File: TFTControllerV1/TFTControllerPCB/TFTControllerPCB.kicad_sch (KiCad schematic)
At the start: 17 parts, among them J1 Conn_01x40, J2 Conn_02x04_Counter_Clockwise, J3 Conn_02x04_Counter_Clockwise, J4 Conn_02x03_Counter_Clockwise, J5 Conn_02x03_Counter_Clockwise, Q1 BSS138, Q2 BSS138, SW1 SW_Push, U1 STM32F107VCTx, U2 XPT2046TS

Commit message: working touch
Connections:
- net XPT_CS: now reaches U2.15 (~{CS})
- net XPT_CS: now also U1.62 (PD15)
- net SWDIO: now reaches U1.72 (PA13)
- net SWCLK: now reaches U1.76 (PA14)
- net SCK: now reaches U1.78 (PC10)
- net MISO: now reaches U1.79 (PC11)
- net MOSI: now reaches U1.80 (PC12)
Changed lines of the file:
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@@
+		)
+	)
+	(global_label "XPT_CS"
+		(shape input)
+		(at 163.83 170.18 180)
+		(fields_autoplaced yes)
+		(effects
+			(font
+				(size 1.27 1.27)
+			)
+			(justify right)
+		)
+		(property "Intersheetrefs" "${INTERSHEET_REFS}"
+			(at 153.9506 170.18 0)
+			(effects
+				(font
+					(size 1.27 1.27)
+				)
+				(justify right)
+				(hide yes)
+			)
+		)
+	)
+	(global_label "MOSI"
+		(shape input)
+		(at 214.63 180.34 0)
+		(fields_autoplaced yes)
+		(effects
+			(font
+				(size 1.27 1.27)
+			)
+			(justify left)
+		)
+		(property "Intersheetrefs" "${INTERSHEET_REFS}"
+			(at 222.2114 180.34 0)
+			(effects
+				(font
+					(size 1.27 1.27)
+				)
+				(justify left)
+				(hide yes)
+			)
+		)
+	)
+	(global_label "MISO"
+		(shape input)
+		(at 214.63 177.8 0)
+		(fields_autoplaced yes)
+		(effects
+			(font
+				(size 1.27 1.27)
+			)
+			(justify left)
+		)
+		(property "Intersheetrefs" "${INTERSHEET_REFS}"
+			(at 222.2114 177.8 0)
+			(effects
+				(font
+					(size 1.27 1.27)
+				)
+				(justify left)
+				(hide yes)
+			)
+		)
+	)
+	(global_label "SWDIO"
+		(shape input)
+		(at 214.63 96.52 0)
+		(fields_autoplaced yes)
+		(effects
+			(font
+				(size 1.27 1.27)
+			)
+			(justify left)
+		)
+		(property "Intersheetrefs" "${INTERSHEET_REFS}"
+			(at 223.4814 96.52 0)
+			(effects
+				(font
+					(size 1.27 1.27)
+				)
+				(justify left)
+				(hide yes)
+			)
+		)
+	)
+	(global_label "SCK"
+		(shape input)
+		(at 214.63 175.26 0)
+		(fields_autoplaced yes)
+		(effects
+			(font
+				(size 1.27 1.27)
+			)
+			(justify left)
+		)
+		(property "Intersheetrefs" "${INTERSHEET_REFS}"
+			(at 221.3647 175.26 0)
+			(effects
+				(font
+					(size 1.27 1.27)
+				)
+				(justify left)
+				(hide yes)
+			)
+		)
+	)
+	(global_label "SWCLK"
+		(shape input)
+		(at 214.63 99.06 0)
+		(fields_autoplaced yes)
+		(effects
+			(font
+				(size 1.27 1.27)
+			)
+			(justify left)
+		)
+		(property "Intersheetrefs" "${INTERSHEET_REFS}"
+			(at 223.8442 99.06 0)
+			(effects
+				(font
+					(size 1.27 1.27)
+				)
+				(justify left)
+				(hide yes)
+			)
+		)
+	)
+	(global_label "XPT_CS"
+		(shape input)
+		(at 241.3 92.71 180)
+		(fields_autoplaced yes)
+		(effects
+			(font
+				(size 1.27 1.27)
+			)
+			(justify right)
+		)
+		(property "Intersheetrefs" "${INTERSHEET_REFS}"
+			(at 231.4206 92.71 0)
+			(effects
+				(font
+					(size 1.27 1.27)
+				)
+				(justify right)
+				(hide yes)
+			)
 		)
 	)

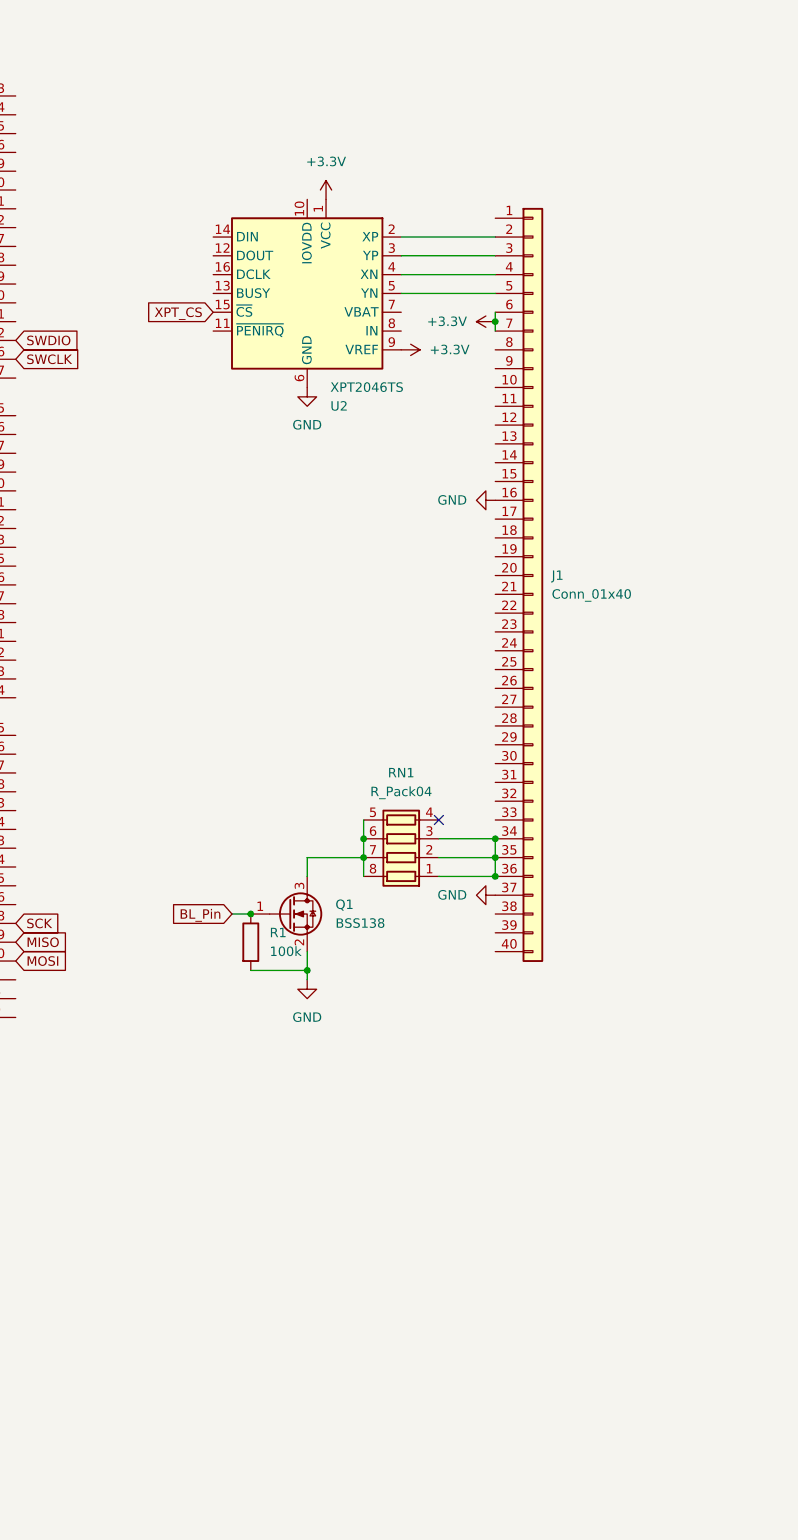
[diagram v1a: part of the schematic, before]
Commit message: migrate project to newer MX version
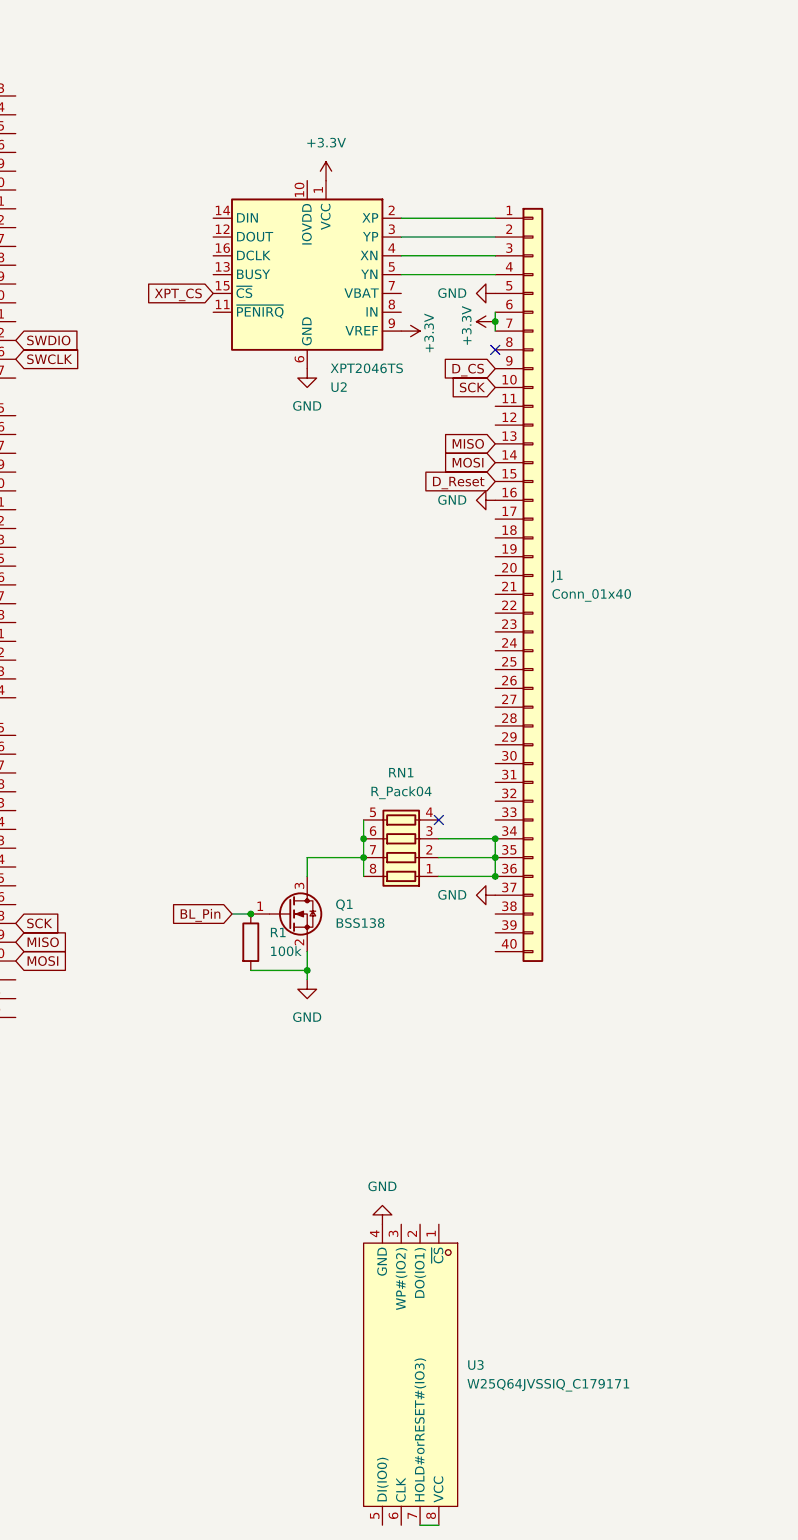
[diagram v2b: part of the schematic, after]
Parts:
- added U3: W25Q64JVSSIQ_C179171, easyeda2kicad:SOIC-8_L5.3-W5.3-P1.27-LS8.0-BL, symbol easyeda2kicad:W25Q64JVSSIQ_C179171
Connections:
- net GND: now also J1.5 (Pin_5), U3.4 (GND)
- net MISO: now also J1.13 (Pin_13)
- net MOSI: now also J1.14 (Pin_14)
- net SCK: now also J1.10 (Pin_10)
- net at U2.2 (XP): now also J1.1 (Pin_1); no longer J1.2 (Pin_2)
- net at U2.3 (YP): now also J1.2 (Pin_2); no longer J1.3 (Pin_3)
- net at U2.4 (XN): now also J1.3 (Pin_3); no longer J1.4 (Pin_4)
- net at U2.5 (YN): now also J1.4 (Pin_4); no longer J1.5 (Pin_5)
- net D_Reset: now reaches J1.15 (Pin_15)
- net D_CS: now reaches J1.9 (Pin_9)
- new net: U3.7 (HOLD#orRESET#(IO3)), U3.8 (VCC)
- no-connect marks 3 -> 4
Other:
- moved on the sheet: U2

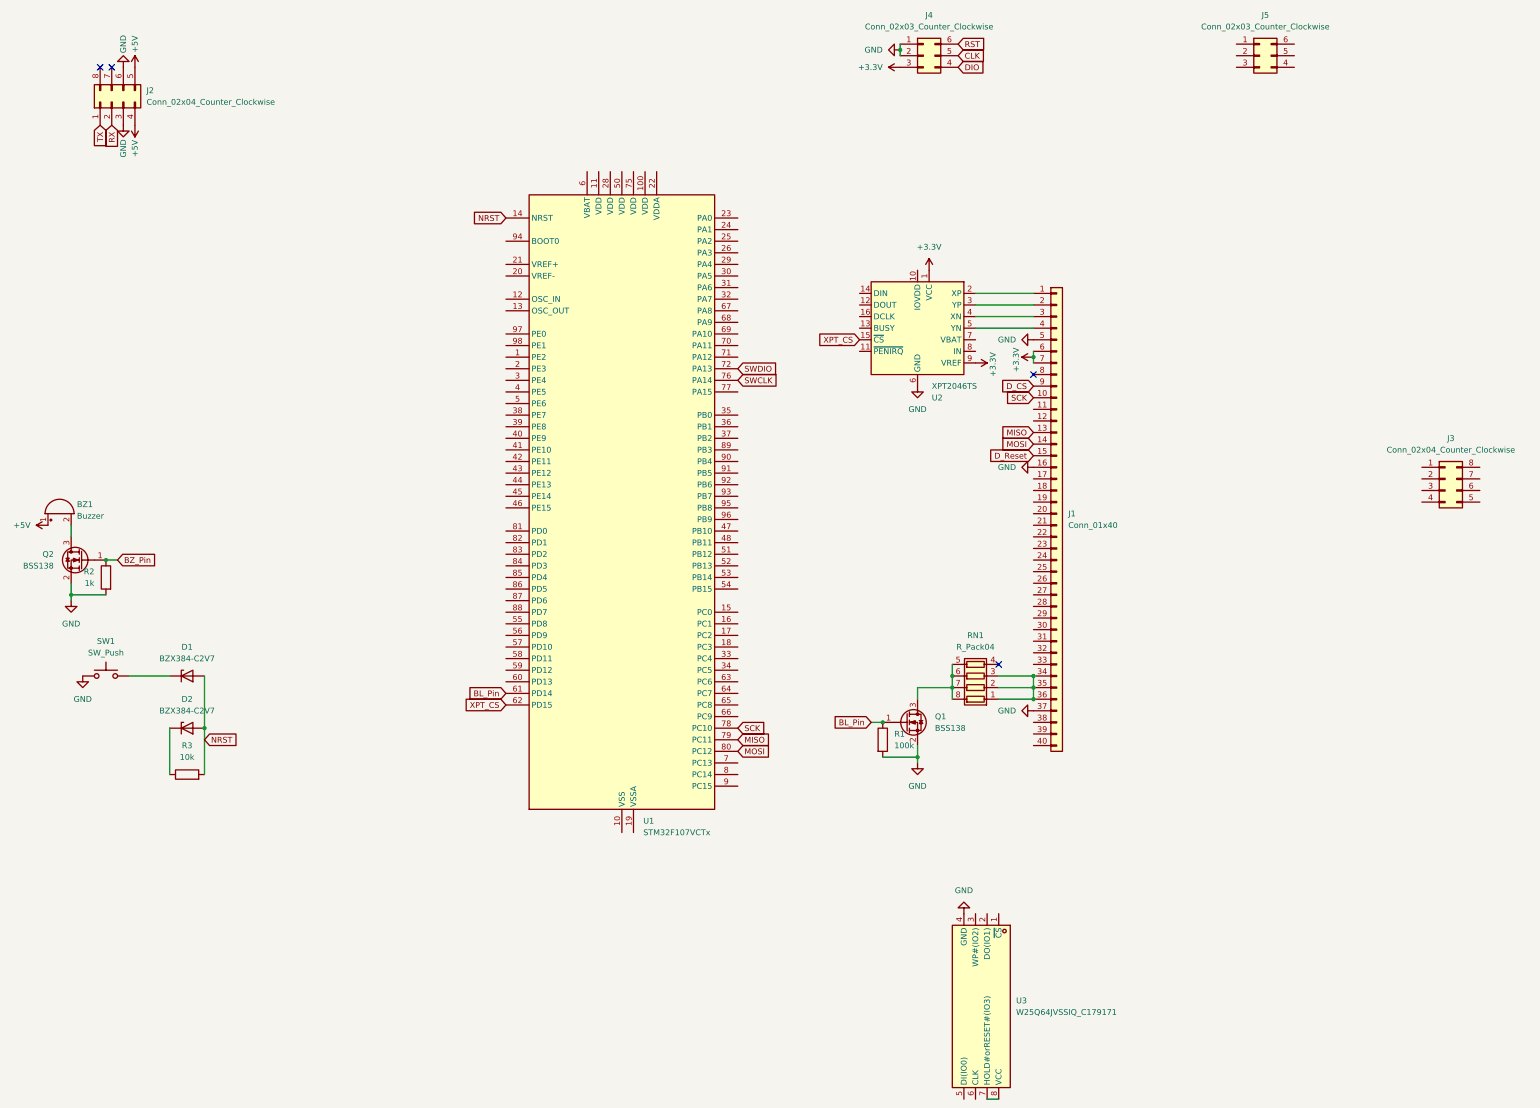
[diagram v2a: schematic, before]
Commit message: add 2SPI
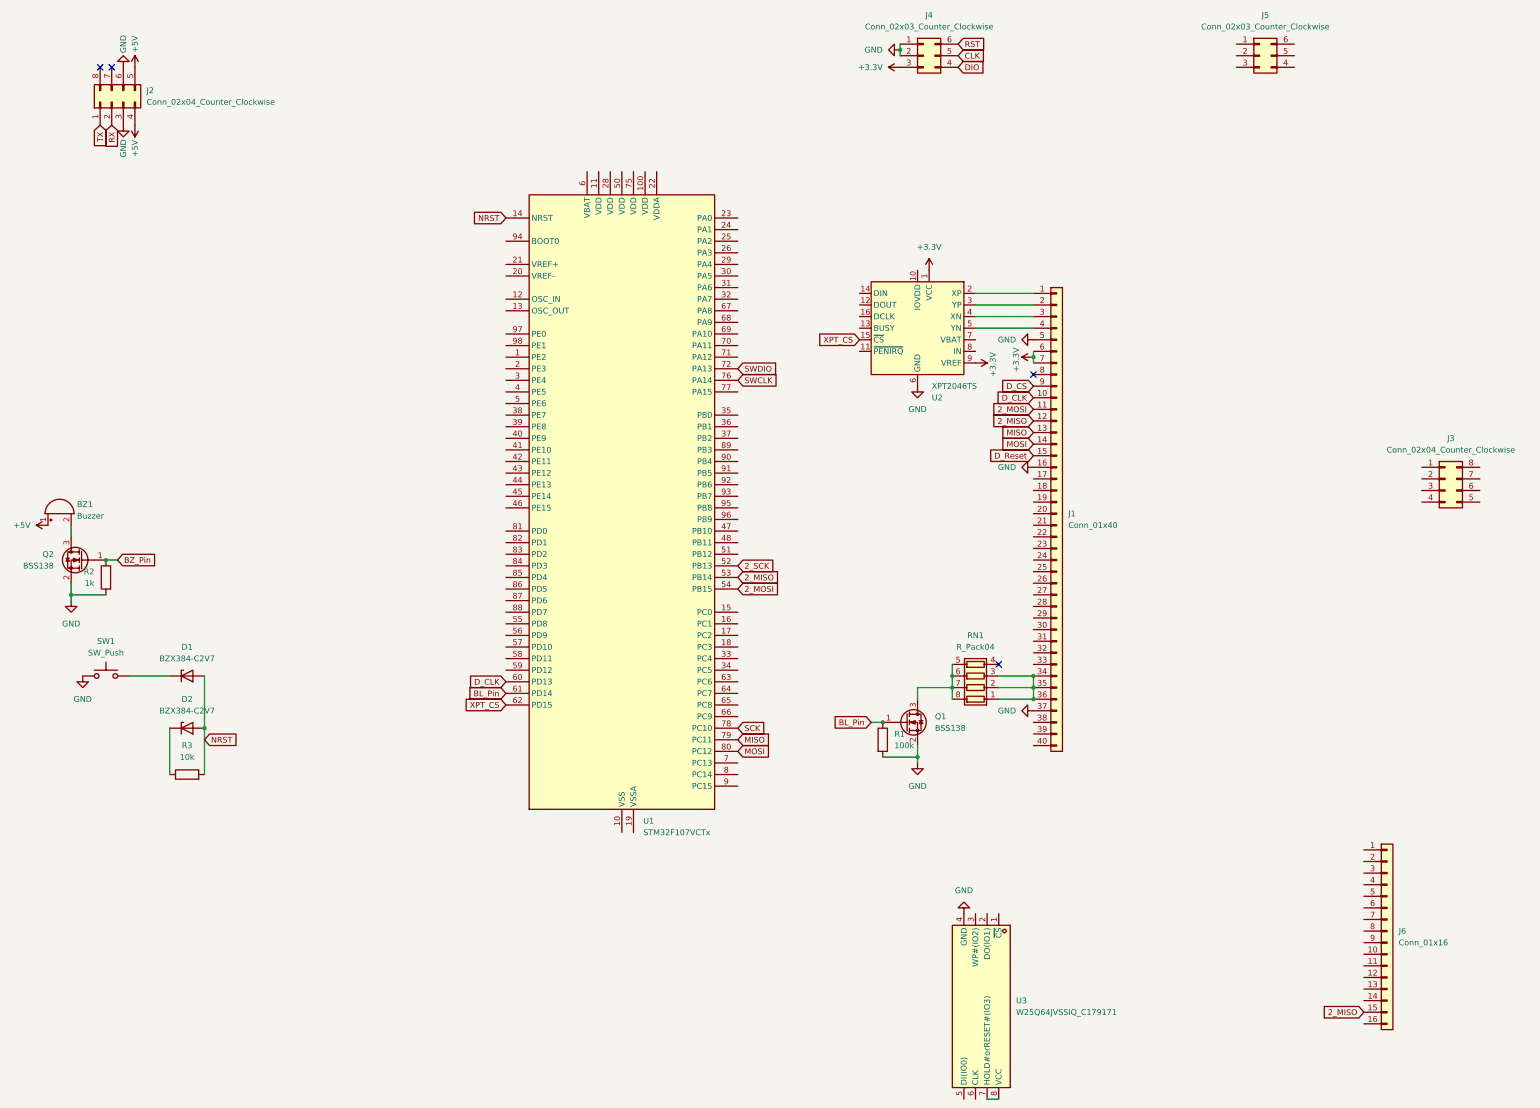
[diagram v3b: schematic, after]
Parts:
- added J6: Conn_01x16, symbol Connector_Generic:Conn_01x16
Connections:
- net SCK: no longer J1.10 (Pin_10)
- net 2_MOSI: now reaches J1.11 (Pin_11)
- net 2_MOSI: now also U1.54 (PB15)
- net 2_MISO: now reaches J1.12 (Pin_12)
- net 2_MISO: now also U1.53 (PB14), J6.15 (Pin_15)
- net 2_SCK: now reaches U1.52 (PB13)
- net D_CLK: now reaches U1.60 (PD13)
- net D_CLK: now also J1.10 (Pin_10)
